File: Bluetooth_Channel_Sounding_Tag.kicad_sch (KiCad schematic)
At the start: 23 parts, among them CN1 S2B-PH-SM4-TB, Q1 MMBT3904-C20526, Q2 AO3401A, Q3 DMN2056U-7, SW1 TS-1088-AR02016, U1 NPM1300-QEAA-R7

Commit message: Add MCU, radio and motion sensor circuitry
Add the nRF54L15 supply filtering and decoupling, 32 MHz and 32.768 kHz crystals, reset circuit, and Tag-Connect SWD/SWO programming interface.

Wire the radio matching network and BGS12WN6 antenna switch, including its control pull-down and RF input DC-blocking capacitor. Add the LIS2DW12 accelerometer, its decoupling, shared I2C connection, and motion interrupt. Connect the nPM1300 interrupt to the MCU and add ESD441 protection to USB VBUS.

Mark all 23 unused MCU pins as intentionally unconnected, including the UART pins now that serial test pads have been dropped. Include the imported component symbols, footprints, and 3D models, and update the project component list.

This records the current schematic progress. The two antenna output branches, matching provisions, antenna geometry and tuning remain unfinished. Other test pads are deferred, and external CC1/CC2 ESD protection is omitted for this revision. PCB layout and final schematic/ERC verification are still pending.
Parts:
- added C10, C11, C12, C13, C22, C25, C26: 100nF, easyeda2kicad:C0201, symbol BCS:CL03A104KP3NNNC
- added C14, C15: 2.2uF, easyeda2kicad:C0201, symbol BCS:GRM033R60J225ME47D
- added C16: 10nF, easyeda2kicad:C0201, symbol BCS:CC0201KRX7R7BB103
- added C17: 2.2nF, easyeda2kicad:C0201, symbol BCS:0201B222K160NT
- added C18: 3.9pF, easyeda2kicad:C0201, symbol BCS:TCC0201COG3R9C500ZT
- added C19: 1.5pF, easyeda2kicad:C0201, symbol BCS:GJM0335C1E1R5WB01D
- added C20: 2pF, easyeda2kicad:C0201, symbol BCS:GJM0335C1E2R0WB01D
- added C21: 0.3pF, easyeda2kicad:C0201, symbol BCS:GJM0335C1ER30WB01D
- added C23: 47pF, easyeda2kicad:C0201, symbol BCS:GRM0335C1H470JA01D
- added C24: 10uF, easyeda2kicad:C0603, symbol BCS:CL10A106MA8NRNC
- added C9: 10uF, easyeda2kicad:C0402, symbol BCS:GRM155R61A106ME11D
- added D1: ESD441DPLR, easyeda2kicad:X2SON-2_L0.6-W0.3-P0.35, symbol BCS:ESD441DPLR
- added J1: Conn_02x03_Odd_Even, Connector:Tag-Connect_TC2030-IDC-NL_2x03_P1.27mm_Vertical, symbol Connector_Generic:Conn_02x03_Odd_Even
- added L2: 4.7uH, easyeda2kicad:L0603, symbol BCS:MLZ1608M4R7WT000
- added L3: BLM03AG121SN1D, easyeda2kicad:L0201, symbol BCS:BLM03AG121SN1D
- added L4: 2.7nH, easyeda2kicad:L0201, symbol BCS:LQP03HQ2N7B02D
- added L5, L6: 3.5nH, easyeda2kicad:L0201, symbol BCS:LQP03HQ3N5B02D
- added R7: 1K, easyeda2kicad:R0201, symbol BCS:0201WMF1001TEE
- added R8: 100K, easyeda2kicad:R0201, symbol BCS:RC0201FR-07100KL
- added R9: 0, easyeda2kicad:R0201, symbol BCS:0201WMF0000TEE
- added U2: NRF54L15-QFAA-R, easyeda2kicad:QFN-48_L6.0-W6.0-P0.40-TL-EP4.6, symbol BCS:NRF54L15-QFAA-R
- added U3: BGS 12WN6 E6327, easyeda2kicad:TSNP-6_L1.1-W0.7-P0.40-BL, symbol BCS:BGS12WN6E6327
- added U4: LIS2DW12TR, easyeda2kicad:LGA-12_L2.0-W2.0-P0.50-BL, symbol BCS:LIS2DW12TR
- added X1: 32MHz, easyeda2kicad:CRYSTAL-SMD_4P-L2.0-W1.6-BL, symbol BCS:ABM11W-32.0000MHZ-8-B1U-T3
- added X2: 32.768KHz, easyeda2kicad:CRYSTAL-SMD_L2.0-W1.2, symbol BCS:CM8V-T1A-32.768KHZ-9PF-20PPM-TB-QC
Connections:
- net GND: now also C10.2, C11.2, C12.2, C13.2, C14.2, C15.2, C16.2, C17.2, C18.2, C19.2, C20.2, C21.2, C22.2, C24.2, C25.2, C26.2, C9.2, D1.2, J1.5 (Pin_5), R8.2, U2.32 (VSS_PA), U2.44 (VSS), U2.49 (EP), U3.2 (GND), U4.5 (NC), U4.6 (GND), U4.7 (RES), U4.8 (GND), X1.2 (GND), X1.4 (GND)
- net PMIC_INT: now also U2.23 (P0.00)
- net SCL: now also U2.8 (P1.07/AIN3/TAMPC), U4.1 (SCL/SPC)
- net SDA: now also U2.7 (P1.06/AIN2/TAMPC), U4.4 (SDA/SDI/SDO)
- net VOUT1: now also C10.1, C11.1, C12.1, C13.1, C22.1, C24.1, C25.1, C26.1, C9.1, J1.1 (Pin_1), U2.10 (VDD), U2.22 (VDD), U2.36 (VDD), U2.47 (VDD), U2.48 (VDD), U3.4 (VDD), U4.10 (VDDIO), U4.2 (CS), U4.3 (SDO/SA0), U4.9 (VDD)
- net at C1.1, U1.21 (VBUS), USB1.A4B9 (VBUS)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: now also D1.1
- new net: C18.1, R7.1, U2.30 (nRESET)
- new net: L4.1, U2.31 (ANT)
- new net: C19.1, L4.2, L5.1
- new net: C15.1, C16.1, C17.1, L3.1, U2.33 (DECRF), U2.43 (DECA)
- new net: U2.1 (P1.00/XL1), X2.1
- new net: U2.2 (P1.01/XL2), X2.2
- new net: C20.1, L5.2, L6.1
- new net: C23.2, U3.5 (RFIN)
- new net ACCEL_INT: U2.24 (P0.01), U4.12 (INT1)
- new net ANT_SEL: R8.1, U2.37 (P1.09/TAMPC), U3.6 (CTRL)
- new net DCC: L2.2, U2.46 (DCC)
- new net DECD: C14.1, L2.1, L3.2, U2.45 (DECD)
- new net NRESET: J1.3 (Pin_3), R7.2
- new net RF: C21.1, C23.1, L6.2
- new net SWDCLK: J1.4 (Pin_4), U2.26 (SWDCLK)
- new net SWDIO: J1.2 (Pin_2), U2.25 (SWDIO)
- new net SWO: J1.6 (Pin_6), U2.18 (P2.07/TRACEDATA[0]/SWO/SPI.DCX)
- new net XC1: U2.34 (XC1), X1.3 (OSC2)
- new net XC2: U2.35 (XC2), X1.1 (OSC1)
- no-connect marks 15 -> 39
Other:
- moved on the sheet: C1, C2, C3, C4, C5, C6, C7, C8, CN1, L1, LED1, Q1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

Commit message: Add antenna matching and prepare the PCB for layout
Add two PCB antenna symbols with separate matching networks and six test
points for power rails and I2C. Add schematic notes explaining the PMIC
configuration, wake button and unpopulated antenna matching components.

Correct the USB-C mounting slots and locating holes, RF switch pads and
courtyard, and SMD attributes on the 0201 passives and low-frequency
crystal. Register the custom footprints in the project-local BCS library
and update their schematic assignments.

Configure the four-layer JLCPCB stack-up, fabrication clearances, track
and via presets, and a component hole-spacing rule. Transfer 67 footprints
and their nets into the PCB and add an initial 35 x 40 mm board outline.

Antenna footprints, component placement and routing remain to be done.
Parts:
- added AE1, AE2: TI_AN043_IFA, symbol Device:Antenna_Shield
- added C27, C28, C29, C30: Tune, BCS:C0201, symbol Device:C
- added R10: 0, BCS:R0201, symbol BCS:0201WMF0000TEE
- added TP1: GND, TestPoint:TestPoint_Pad_D1.0mm, symbol Connector:TestPoint
- added TP2: VBAT, TestPoint:TestPoint_Pad_D1.0mm, symbol Connector:TestPoint
- added TP3: VSYS, TestPoint:TestPoint_Pad_D1.0mm, symbol Connector:TestPoint
- added TP4: VOUT1, TestPoint:TestPoint_Pad_D1.0mm, symbol Connector:TestPoint
- added TP5: SCL, TestPoint:TestPoint_Pad_D1.0mm, symbol Connector:TestPoint
- added TP6: SDA, TestPoint:TestPoint_Pad_D1.0mm, symbol Connector:TestPoint
- C1, C2, C24, C3, C4, C5, C6: footprint easyeda2kicad:C0603 -> BCS:C0603
- C10, C11, C12, C13, C14, C15, C16, C17, C18, C19, C20, C21, C22, C23, C25, C26, C7: footprint easyeda2kicad:C0201 -> BCS:C0201
- C8, C9: footprint easyeda2kicad:C0402 -> BCS:C0402
- CN1: footprint easyeda2kicad:CONN-SMD_P2.00_S2B-PH-SM4-TB-LF-SN -> BCS:CONN-SMD_P2.00_S2B-PH-SM4-TB-LF-SN
- D1: footprint easyeda2kicad:X2SON-2_L0.6-W0.3-P0.35 -> BCS:X2SON-2_L0.6-W0.3-P0.35
- L1: footprint easyeda2kicad:L0805 -> BCS:L0805
- L2: footprint easyeda2kicad:L0603 -> BCS:L0603
- L3, L4, L5, L6: footprint easyeda2kicad:L0201 -> BCS:L0201
- LED1: footprint easyeda2kicad:LED-SMD_L0.7-W0.4-RD_GREEN-1 -> BCS:LED-SMD_L0.7-W0.4-RD_GREEN-1
- Q1: footprint easyeda2kicad:SOT-23-3_L2.9-W1.3-P1.90-LS2.4-BR -> BCS:SOT-23-3_L2.9-W1.3-P1.90-LS2.4-BR
- Q2: footprint easyeda2kicad:SOT-23_L2.9-W1.3-P1.90-LS2.4-BR -> BCS:SOT-23_L2.9-W1.3-P1.90-LS2.4-BR
- Q3: footprint easyeda2kicad:SOT-23-3_L2.9-W1.6-P1.90-LS2.8-BR -> BCS:SOT-23-3_L2.9-W1.6-P1.90-LS2.8-BR
- R1, R2, R3, R4, R5, R6, R7, R8, R9: footprint easyeda2kicad:R0201 -> BCS:R0201
- SW1: footprint easyeda2kicad:SW-SMD_L3.9-W3.0-P4.45 -> BCS:SW-SMD_L3.9-W3.0-P4.45
- U1: footprint easyeda2kicad:QFN-32_L5.0-W5.0-P0.50-TL-EP3.5 -> BCS:QFN-32_L5.0-W5.0-P0.50-TL-EP3.5
- U2: footprint easyeda2kicad:QFN-48_L6.0-W6.0-P0.40-TL-EP4.6 -> BCS:QFN-48_L6.0-W6.0-P0.40-TL-EP4.6
- U3: footprint easyeda2kicad:TSNP-6_L1.1-W0.7-P0.40-BL -> BCS:TSNP-6_L1.1-W0.7-P0.40-BL
- U4: footprint easyeda2kicad:LGA-12_L2.0-W2.0-P0.50-BL -> BCS:LGA-12_L2.0-W2.0-P0.50-BL
- USB1: footprint easyeda2kicad:USB-C-SMD_GT-USB-7010E-1 -> BCS:USB-C-SMD_GT-USB-7010E-1
- X1: footprint easyeda2kicad:CRYSTAL-SMD_4P-L2.0-W1.6-BL -> BCS:CRYSTAL-SMD_4P-L2.0-W1.6-BL
- X2: footprint easyeda2kicad:CRYSTAL-SMD_L2.0-W1.2 -> BCS:CRYSTAL-SMD_L2.0-W1.2
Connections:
- net GND: now also AE1.2 (Shield), AE2.2 (Shield), C27.2, C28.2, C29.1, C30.1, TP1.1
- net SCL: now also TP5.1
- net SDA: now also TP6.1
- net VBAT: now also TP2.1
- net VOUT1: now also TP4.1
- net VSYS: now also TP3.1
- net at R9.1: now also U3.3 (RF1), C28.1
- net at R9.2: now also AE1.1 (A), C27.1
- net at U3.1 (RF2): now also C29.2, R10.1
- new net: AE2.1 (A), C30.2, R10.2
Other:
- moved on the sheet: C10, C11, C12, C13, C14, C15, C16, C17, C18, C19, C20, C21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

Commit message: Place components and start routing the PCB
Expand the board to 35 x 42.5 mm with 2 mm rounded corners. Add the M2
mounting hole and two antenna reservations, and arrange the power, MCU,
sensor, RF and programming components.

Add initial routing for the USB input, battery protection, PMIC power
connections, I2C, button, testpoints and 32 kHz crystal. Reposition L1 and
C6 to shorten the BUCK1 switch connection and improve the output routing.
Include the updated project settings and repositioned schematic drawing.

This is an in-progress layout checkpoint. Ground planes and returns,
remaining supply and bus connections, debug, the 32 MHz crystal and RF
and antenna routing still need work. ERC and DRC were not run for this
checkpoint.
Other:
- moved on the sheet: AE1, AE2, C1, C10, C11, C12, C13, C14, C15, C16, C17, C18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

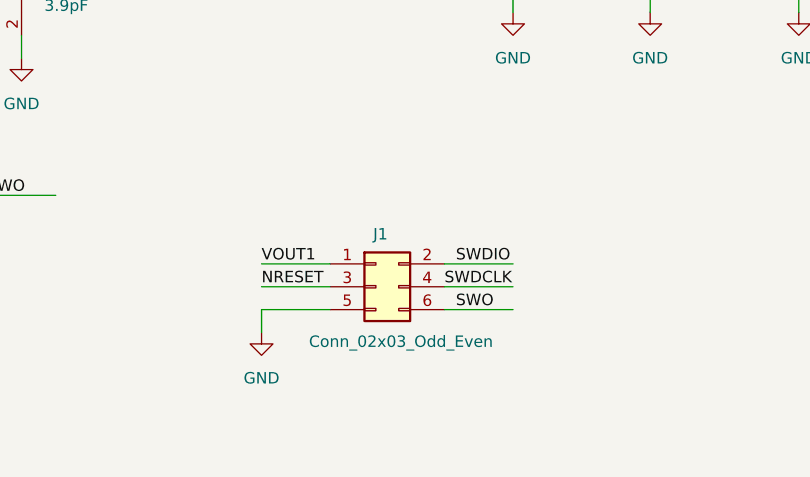
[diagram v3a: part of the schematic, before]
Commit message: Route the RF paths and add PhaseTag branding
Add ground pours and RF grounding, route both PCB antennas through the RF switch, and define the 50-ohm RF routing profile.

Refine power, signal and debugger routing, assign the antenna footprints in the schematic, and add the PhaseTag logo, product name, designer credit and revision marking.
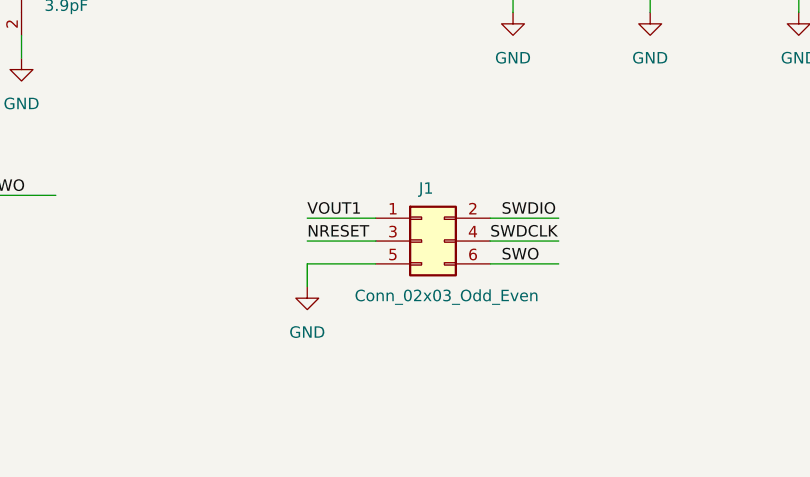
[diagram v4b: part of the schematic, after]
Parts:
- AE1: footprint (none) -> RF_Antenna:Texas_SWRA117D_2.4GHz_Left
- AE2: footprint (none) -> RF_Antenna:Texas_SWRA117D_2.4GHz_Right
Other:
- moved on the sheet: J1
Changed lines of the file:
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@@
 	(wire
 		(pts
-			(xy 379.73 289.56) (xy 387.35 289.56)
+			(xy 384.81 284.48) (xy 392.43 284.48)
 		)
 		(stroke
@@
 	(wire
 		(pts
-			(xy 367.03 289.56) (xy 359.41 289.56)
+			(xy 372.11 284.48) (xy 364.49 284.48)
 		)
 		(stroke
@@
 	(wire
 		(pts
-			(xy 359.41 289.56) (xy 359.41 292.1)
+			(xy 364.49 284.48) (xy 364.49 287.02)
 		)
 		(stroke
@@
 	(wire
 		(pts
-			(xy 359.41 284.48) (xy 367.03 284.48)
+			(xy 364.49 279.4) (xy 372.11 279.4)
 		)
 		(stroke
@@
 	(wire
 		(pts
-			(xy 379.73 284.48) (xy 387.35 284.48)
+			(xy 384.81 279.4) (xy 392.43 279.4)
 		)
 		(stroke
@@
 	(wire
 		(pts
-			(xy 359.41 287.02) (xy 367.03 287.02)
+			(xy 364.49 281.94) (xy 372.11 281.94)
 		)
 		(stroke
@@
 	(wire
 		(pts
-			(xy 379.73 287.02) (xy 387.35 287.02)
+			(xy 384.81 281.94) (xy 392.43 281.94)
 		)
 		(stroke
@@
 	)
 	(label "NRESET"
-		(at 359.41 287.02 0)
+		(at 364.49 281.94 0)
 		(effects
 			(font
@@
 	)
 	(label "SWO"
-		(at 381 289.56 0)
+		(at 386.08 284.48 0)
 		(effects
 			(font
@@
 	)
 	(label "VOUT1"
-		(at 359.41 284.48 0)
+		(at 364.49 279.4 0)
 		(effects
 			(font
@@
 	)
 	(label "SWDIO"
-		(at 381 284.48 0)
+		(at 386.08 279.4 0)
 		(effects
 			(font
@@
 	)
 	(label "SWDCLK"
-		(at 379.73 287.02 0)
+		(at 384.81 281.94 0)
 		(effects
 			(font
@@
 			)
 		)
-		(property "Footprint" ""
+		(property "Footprint" "RF_Antenna:Texas_SWRA117D_2.4GHz_Right"
 			(at 521.97 224.79 0)
 			(hide yes)
@@
 			)
 		)
-		(property "Footprint" ""
+		(property "Footprint" "RF_Antenna:Texas_SWRA117D_2.4GHz_Left"
 			(at 521.97 252.73 0)
 			(hide yes)
@@
 	(symbol
 		(lib_id "Connector_Generic:Conn_02x03_Odd_Even")
-		(at 372.11 287.02 0)
+		(at 377.19 281.94 0)
 		(unit 1)
 		(body_style 1)
@@
 		(dnp no)
 		(property "Reference" "J1"
-			(at 372.618 281.178 0)
+			(at 377.698 276.098 0)
 			(show_name no)
 			(do_not_autoplace no)
@@
 		)
 		(property "Value" "Conn_02x03_Odd_Even"
-			(at 374.904 293.116 0)
+			(at 379.984 288.036 0)
 			(show_name no)
 			(do_not_autoplace no)
@@
 		)
 		(property "Footprint" "Connector:Tag-Connect_TC2030-IDC-NL_2x03_P1.27mm_Vertical"
-			(at 372.11 287.02 0)
+			(at 377.19 281.94 0)
 			(hide yes)
 			(show_name no)
@@
 		)
 		(property "Datasheet" ""
-			(at 372.11 287.02 0)
+			(at 377.19 281.94 0)
 			(hide yes)
 			(show_name no)
@@
 		)
 		(property "Description" "Generic connector, double row, 02x03, odd/even pin numbering scheme (row 1 odd numbers, row 2 even numbers), script generated (kicad-library-utils/schlib/autogen/connector/)"
-			(at 372.11 287.02 0)
+			(at 377.19 281.94 0)
 			(hide yes)
 			(show_name no)
@@
 	(symbol
 		(lib_id "power:GND")
-		(at 359.41 292.1 0)
+		(at 364.49 287.02 0)
 		(unit 1)
 		(body_style 1)
@@
 		(fields_autoplaced yes)
 		(property "Reference" "#PWR029"
-			(at 359.41 298.45 0)
+			(at 364.49 293.37 0)
 			(hide yes)
 			(show_name no)
@@
 		)
 		(property "Value" "GND"
-			(at 359.41 297.18 0)
+			(at 364.49 292.1 0)
 			(show_name no)
 			(do_not_autoplace no)
@@
 		)
 		(property "Footprint" ""
-			(at 359.41 292.1 0)
+			(at 364.49 287.02 0)
 			(hide yes)
 			(show_name no)
@@
 		)
 		(property "Datasheet" ""
-			(at 359.41 292.1 0)
+			(at 364.49 287.02 0)
 			(hide yes)
 			(show_name no)
@@
 		)
 		(property "Description" "Power symbol creates a global label with name \"GND\" , ground"
-			(at 359.41 292.1 0)
+			(at 364.49 287.02 0)
 			(hide yes)
 			(show_name no)
